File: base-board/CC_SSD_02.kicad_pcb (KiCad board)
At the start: 2 copper layers, 66 x 58.4 mm, 42 parts, among them IC1 ATTINY1634-SU, P1 WF2R, P2 BH10S, P3 BH10R, P4 PN1x3, P5 WF3R, P6 WF2R, Q1 DTC144TKA, Q2 DTC144TKA, SW1 TS-06E, SW2 TS-06E, U1 MCP1701AT-3302I/CB, U2 MCP1802T-3302I/OT

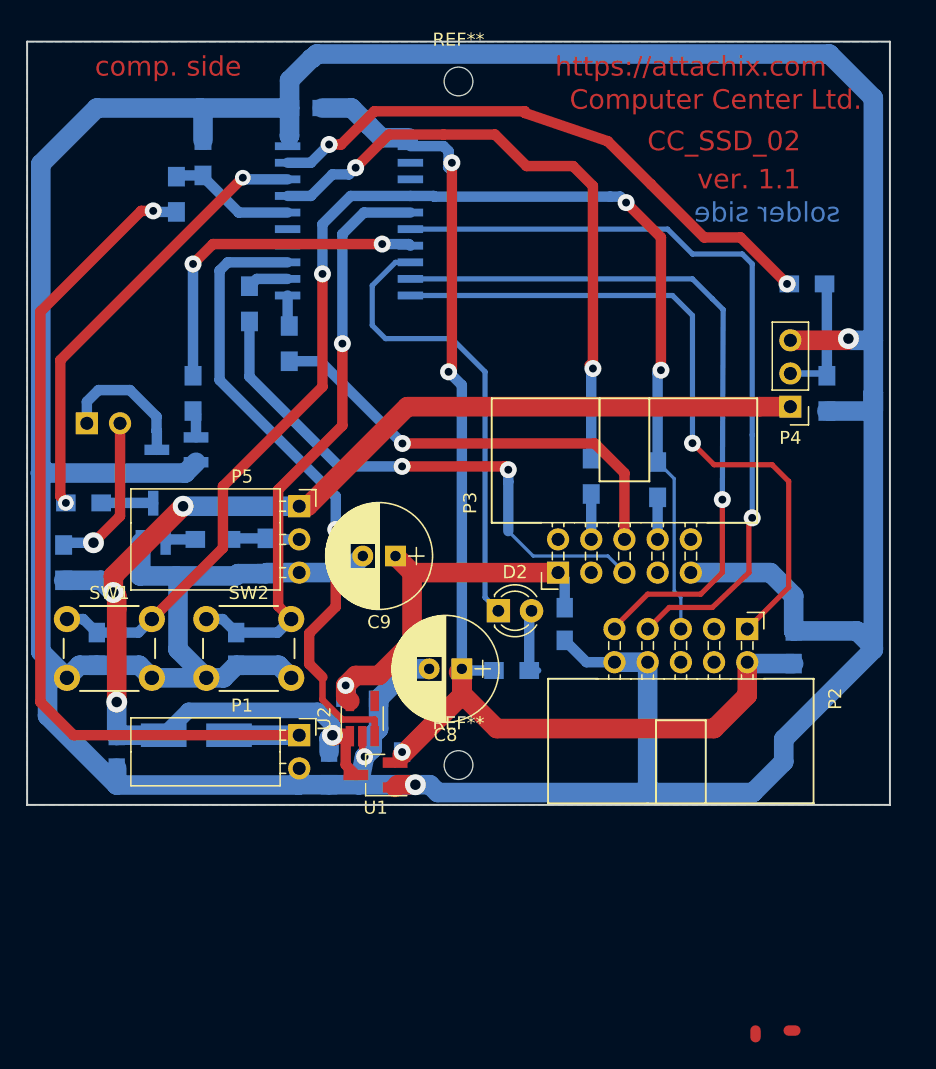
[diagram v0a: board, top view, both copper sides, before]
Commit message: Moved smoke detector header more to the center. Reverted header for Attiny programmer to be straight.
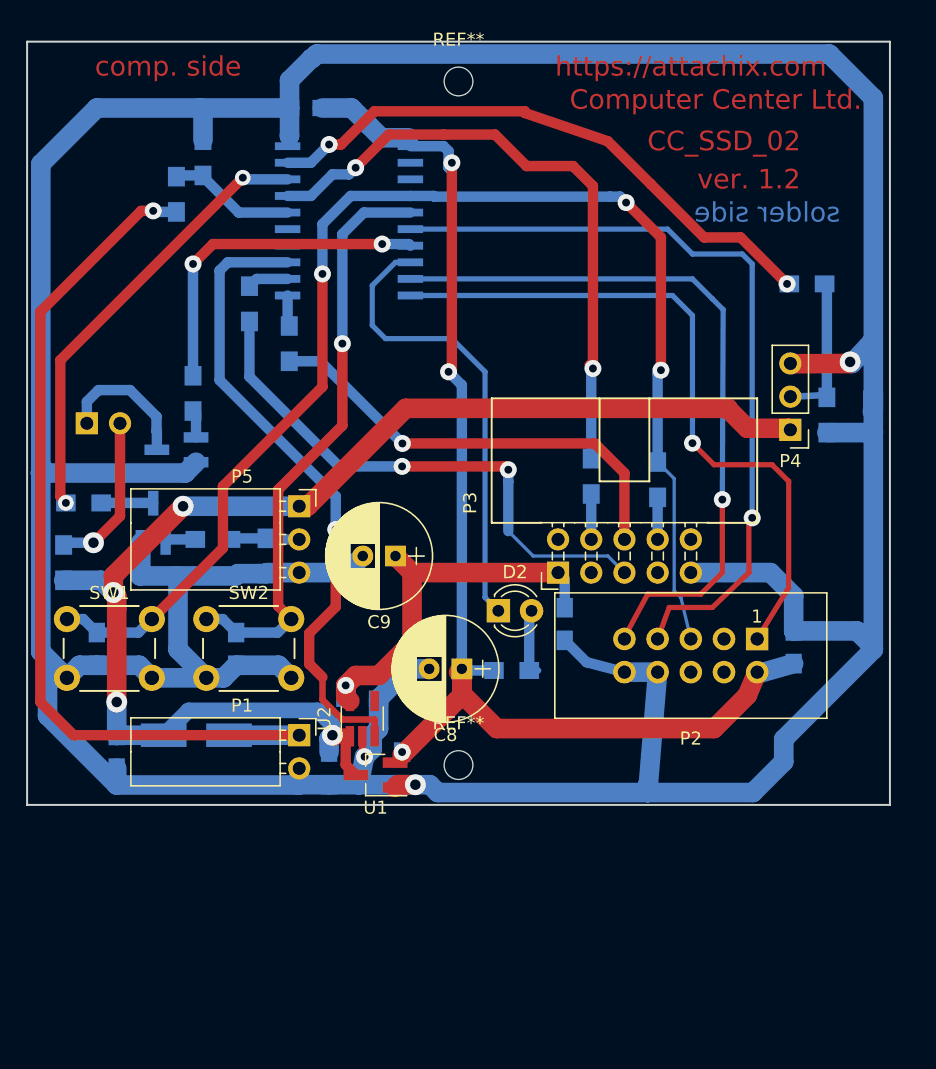
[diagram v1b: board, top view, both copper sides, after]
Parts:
- P2: footprint CC_Footprint:BH10R -> CC_Footprint:IDC_Header_Straight_10pins
- moved P4 1.77 mm to (172.7, 100.8)
- moved R11 1.65 mm to (175.5, 99.7)
- moved P2 1.08 mm to (170.2, 116.8), turned to 180 degrees
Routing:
- net Net-(P4-Pad2): track 10.2 -> 11.9 mm
- net +3V3: track 96.4 -> 95.2 mm
- net GND: track 359.4 -> 360.4 mm
- net (no net): track 1.02 -> 0.00 mm
- net Net-(C10-Pad1): track 102.0 -> 102.9 mm
- net VAA: track 98.0 -> 98.7 mm
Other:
- board text added: "ver. 1.2"
- board text removed: "ver. 1.1"

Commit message: Added new version of the base board with fixes for the connectors and LED moved closer to the ring.
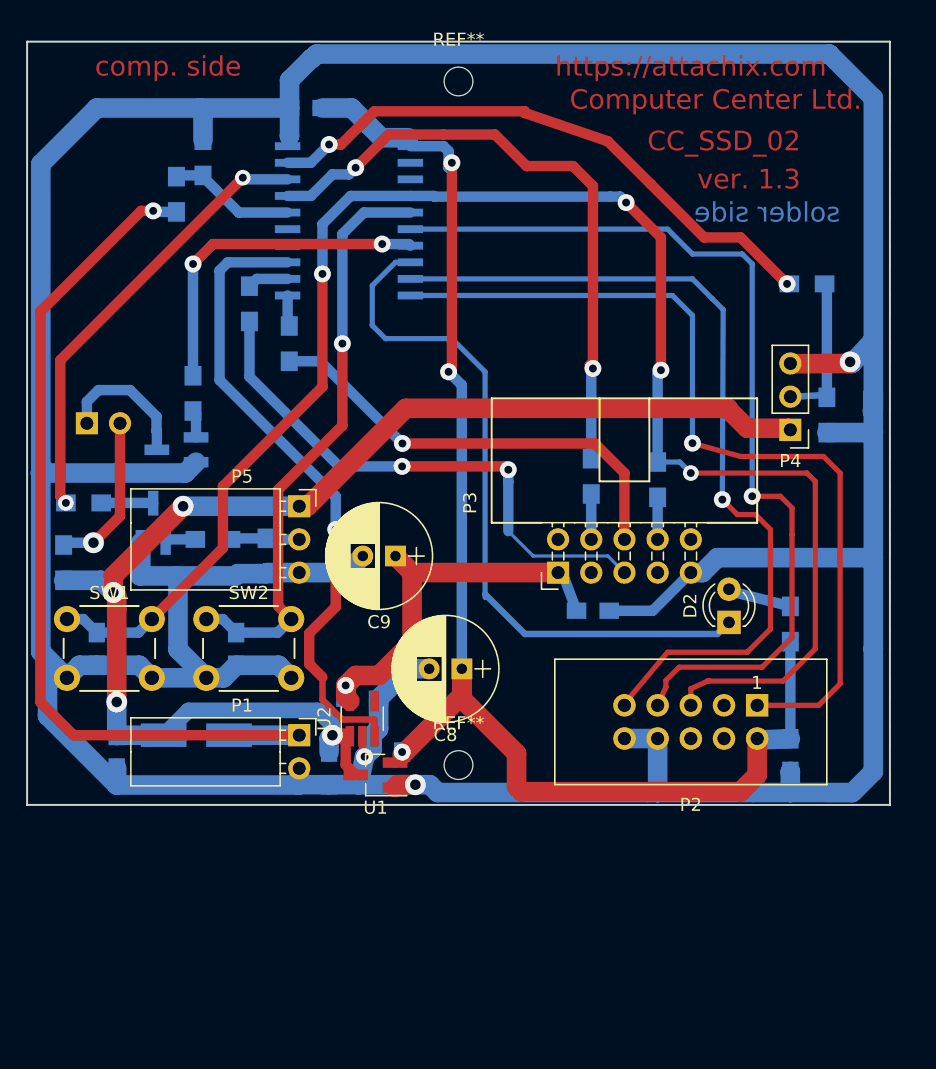
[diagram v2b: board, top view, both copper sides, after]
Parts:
- moved R14 21.6 mm to (172.7, 115.7), turned to 90 degrees
- moved D2 17.7 mm to (168.0, 115.6), turned to 90 degrees
- moved C6 8.26 mm to (172.7, 125.7), turned to 270 degrees
- moved P2 5.08 mm to (170.2, 121.9)
- moved C7 2.39 mm to (157.6, 114.7), turned to 0 degrees
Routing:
- net Net-(C10-Pad1): track 102.9 -> 126.1 mm, vias 3 -> 4
- net Net-(D2-Pad1): track 35.5 -> 54.4 mm
- net Net-(IC1-Pad20): track 53.3 -> 67.1 mm
- net +3V3: track 95.2 -> 106.3 mm
- net Net-(IC1-Pad16): track 60.7 -> 71.4 mm
- net Net-(IC1-Pad19): track 55.3 -> 65.6 mm
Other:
- board text added: "ver. 1.3"
- board text removed: "ver. 1.2"
